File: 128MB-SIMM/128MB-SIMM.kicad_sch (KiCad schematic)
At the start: 6 parts

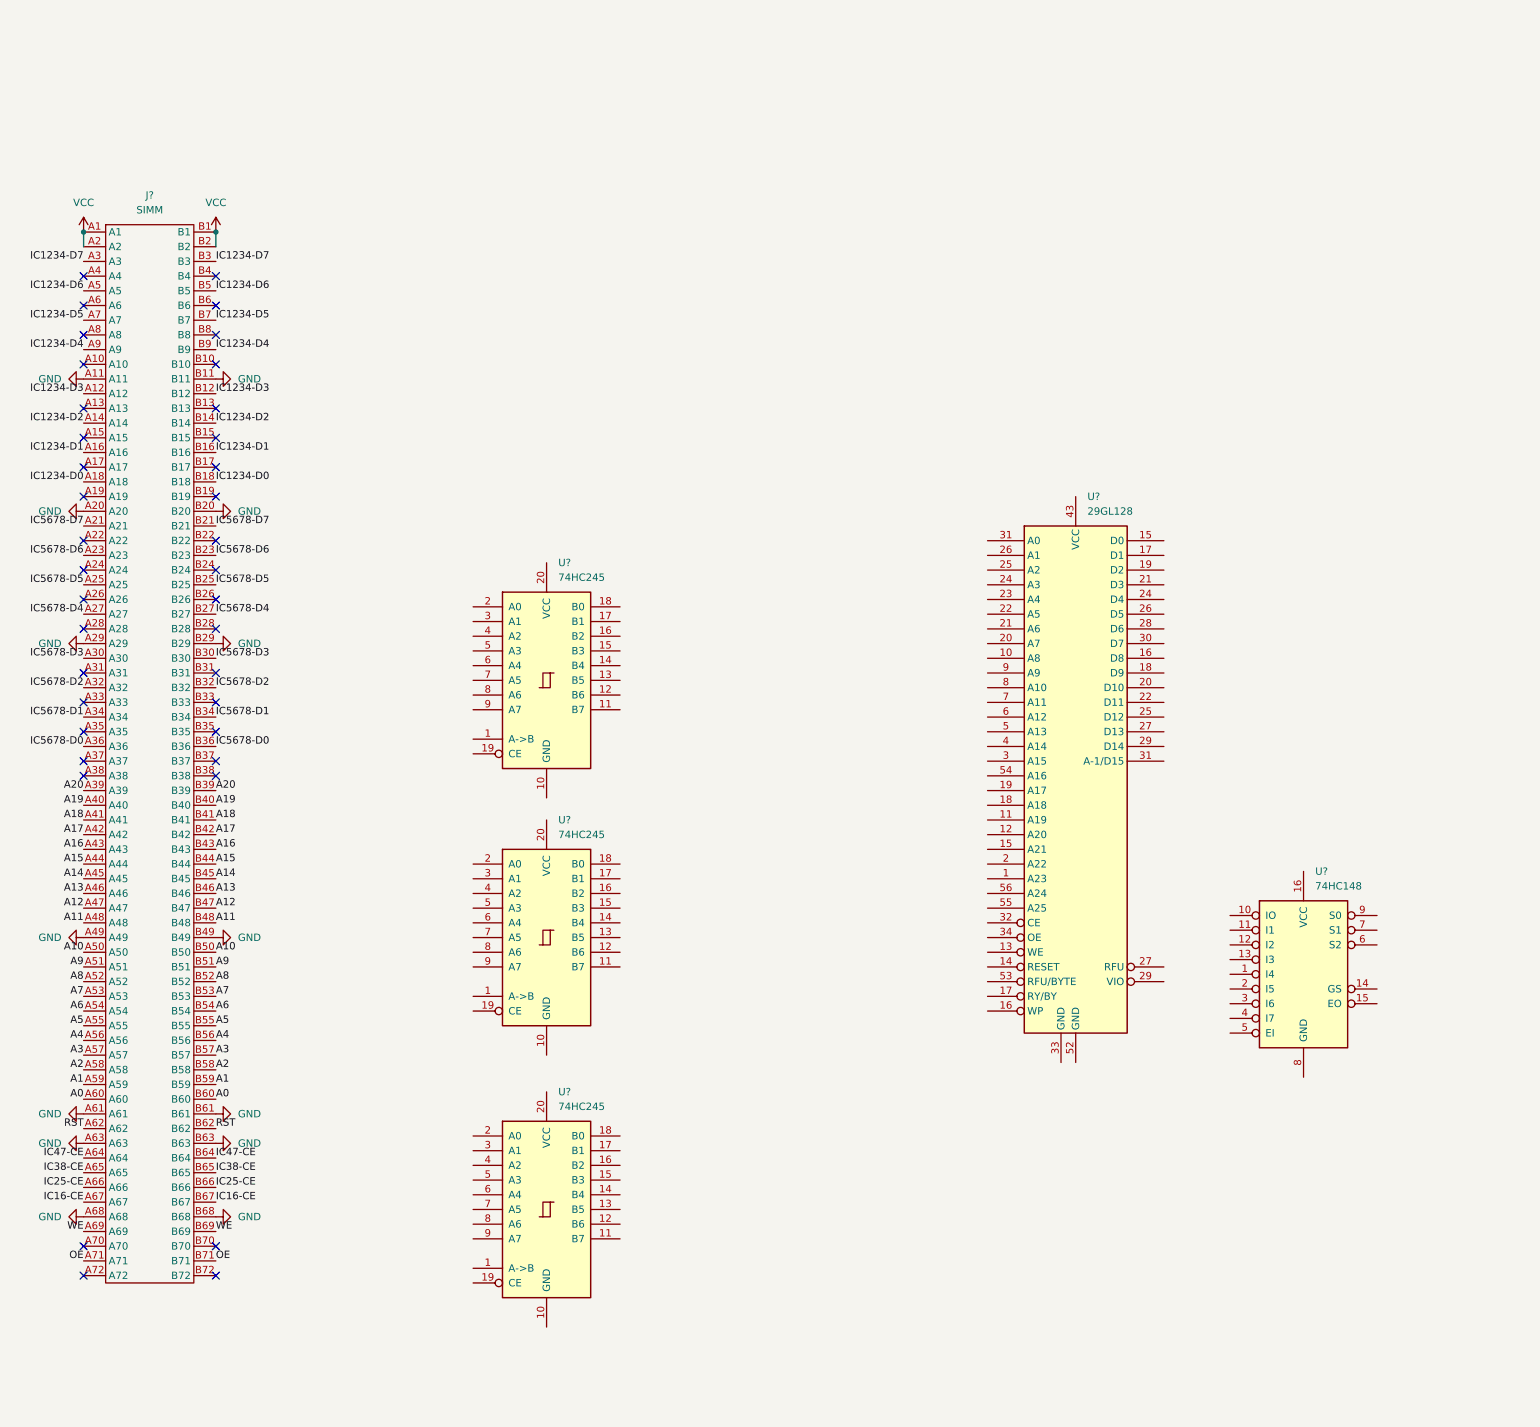
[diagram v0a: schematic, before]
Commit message: Updated 128 SIMM for release
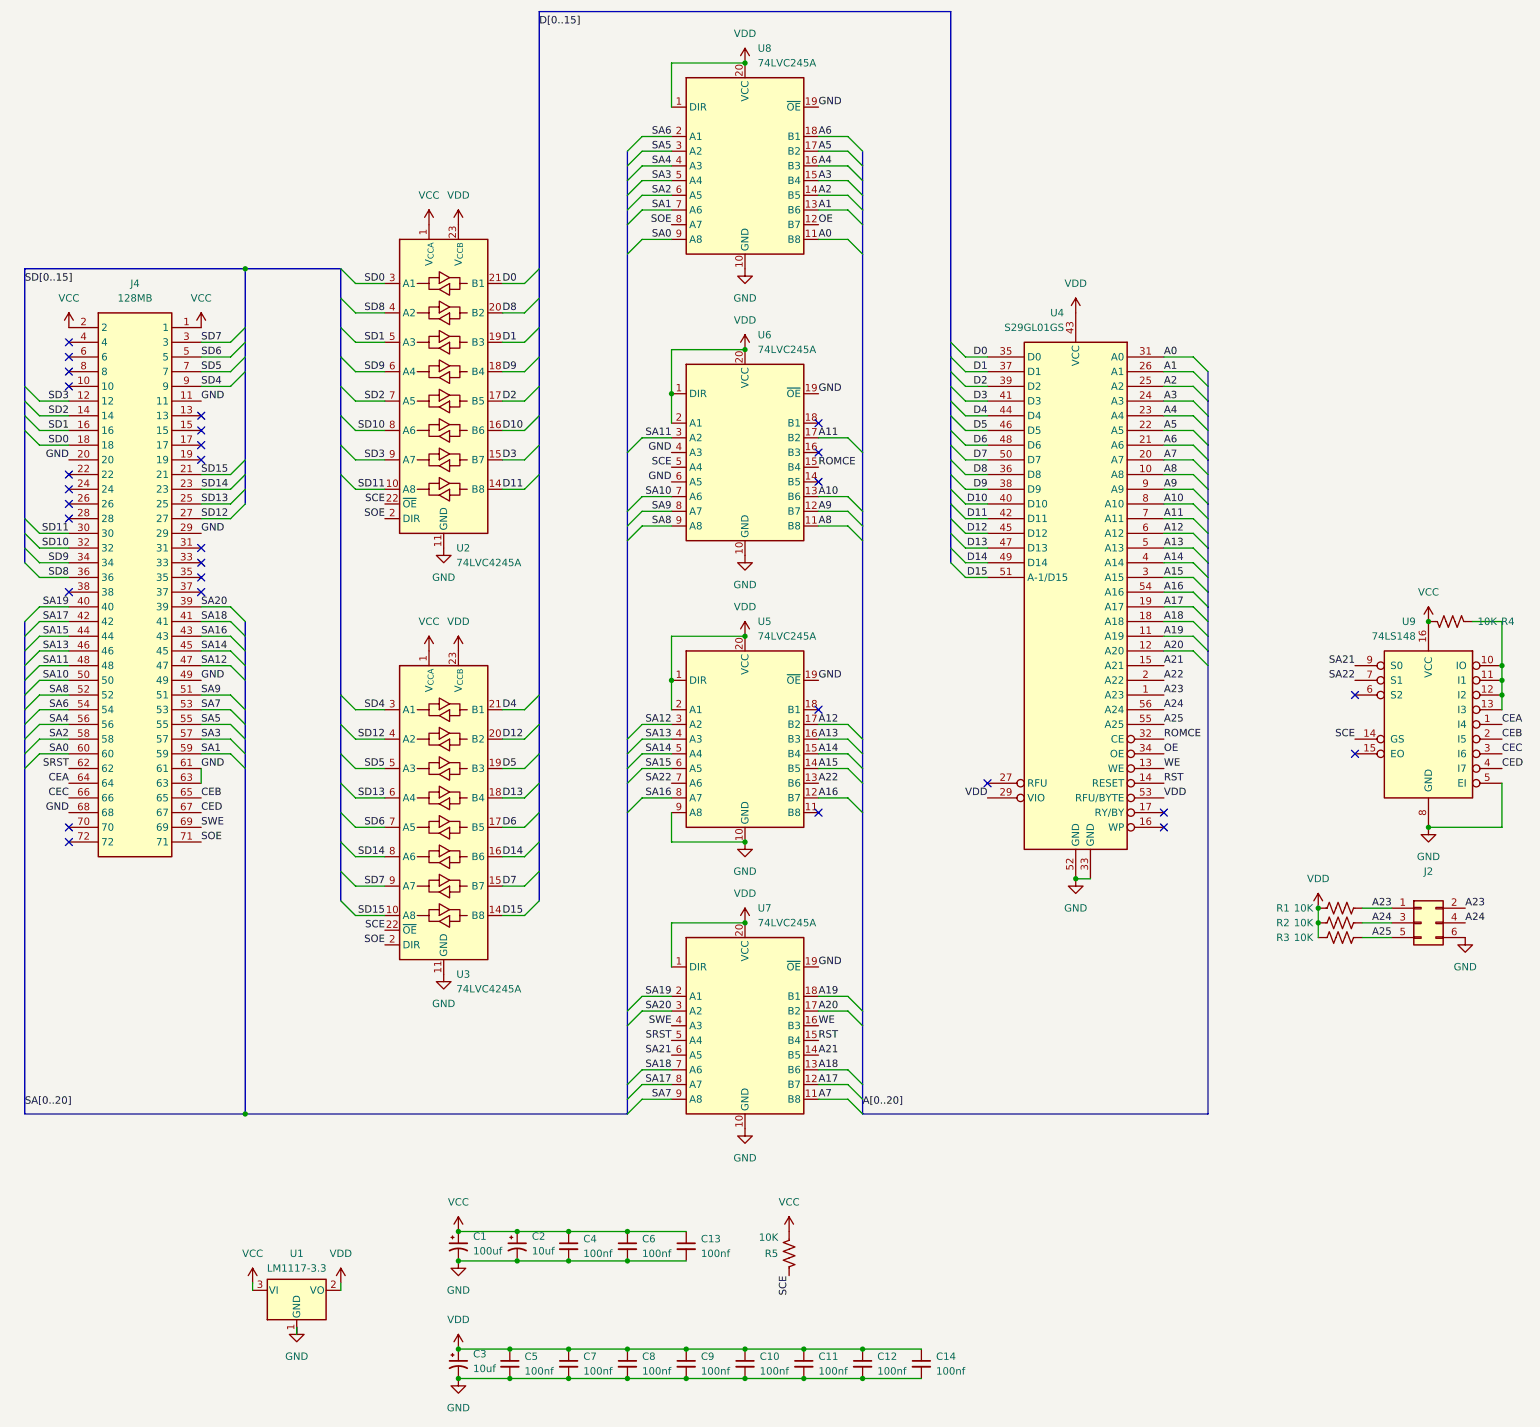
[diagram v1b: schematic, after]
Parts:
- removed J?: SIMM, symbol CPS3:SIMM
- added C1: 100uf, Capacitor_Tantalum_SMD:CP_EIA-3528-12_Kemet-T, symbol Device:C_Polarized_Small_US
- added C10, C11, C12, C13, C14, C4, C5, C6, C7, C8, C9: 100nf, Capacitor_SMD:C_0603_1608Metric, symbol Device:C_Small
- added C2, C3: 10uf, Capacitor_Tantalum_SMD:CP_EIA-3216-10_Kemet-I, symbol Device:C_Polarized_Small_US
- added J2: Conn_02x03_Odd_Even, Connector_PinSocket_1.27mm:PinSocket_2x03_P1.27mm_Horizontal, symbol Connector_Generic:Conn_02x03_Odd_Even
- added J4: 128MB, CPS3:SIMM_EDGE, symbol 5822030-3:5822030-3
- added R1, R2, R3, R4, R5: 10K, Resistor_SMD:R_0603_1608Metric, symbol Device:R_US
- added U1: LM1117-3.3, Package_TO_SOT_SMD:SOT-223-3_TabPin2, symbol Regulator_Linear:AMS1117-3.3
- added U2, U3: 74LVC4245A, Package_SO:TSSOP-24_4.4x7.8mm_P0.65mm, symbol Logic_LevelTranslator:SN74LVC8T245
- added U8: 74LVC245A, Package_SO:TSSOP-20_4.4x6.5mm_P0.65mm, symbol Logic_LevelTranslator:SN74LVC245APW
- U4: renamed from U?; value 29GL128 -> S29GL01GS; LCSC (none) -> C2064354
- U5, U6, U7: renamed from U?; value 74HC245 -> 74LVC245A; footprint (none) -> Package_SO:TSSOP-20_4.4x6.5mm_P0.65mm; symbol 74xx:74HC245 -> Logic_LevelTranslator:SN74LVC245APW; LCSC (none) -> C7848
- U9: renamed from U?; value 74HC148 -> 74LS148; footprint (none) -> Package_SO:SOIC-16_3.9x9.9mm_P1.27mm; symbol CPS3:74HC148 -> 74xx:74LS148; LCSC (none) -> C2674594
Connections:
- net A0: now also U4.31 (A0), U8.11 (B8)
- net A1: now also U4.26 (A1), U8.13 (B6)
- net A10: now also U4.8 (A10), U6.13 (B6)
- net A11: now also U4.7 (A11), U6.17 (B2)
- net A12: now also U4.6 (A12), U5.17 (B2)
- net A13: now also U4.5 (A13), U5.16 (B3)
- net A14: now also U4.4 (A14), U5.15 (B4)
- net A15: now also U4.3 (A15), U5.14 (B5)
- net A16: now also U4.54 (A16), U5.12 (B7)
- net A17: now also U4.19 (A17), U7.12 (B7)
- net A18: now also U4.18 (A18), U7.13 (B6)
- net A19: now also U4.11 (A19), U7.18 (B1)
- net A2: now also U4.25 (A2), U8.14 (B5)
- net A20: now also U4.12 (A20), U7.17 (B2)
- net A3: now also U4.24 (A3), U8.15 (B4)
- net A4: now also U4.23 (A4), U8.16 (B3)
- net A5: now also U4.22 (A5), U8.17 (B2)
- net A6: now also U4.21 (A6), U8.18 (B1)
- net A7: now also U4.20 (A7), U7.11 (B8)
- net A8: now also U4.10 (A8), U6.11 (B8)
- net A9: now also U4.9 (A9), U6.12 (B7)
- net GND: now also U4.33 (GND), U4.52 (GND), U5.10 (GND), U5.19 (~{OE}), U5.9 (A8), U6.10 (GND), U6.19 (~{OE}), U6.4 (A3), U6.6 (A5), U7.10 (GND), U7.19 (~{OE}), U9.5 (EI), U9.8 (GND), C1.2, C10.2, C11.2, C12.2, C13.2, C14.2, C2.2, C3.2, C4.2, C5.2, C6.2, C7.2, C8.2, C9.2, J2.6 (Pin_6), J4.11, J4.20, J4.29, J4.49, J4.61, J4.63, J4.68, U1.1 (GND), U2.11 (GND), U2.12 (GND), U2.13 (GND), U3.11 (GND), U3.12 (GND), U3.13 (GND), U8.10 (GND), U8.19 (~{OE})
- net OE: now also U4.34 (OE), U8.12 (B7)
- net RST: now also U4.14 (RESET), U7.15 (B4)
- net VCC: now also U9.16 (VCC), C1.1, C13.1, C2.1, C4.1, C6.1, J4.1, J4.2, R4.2, R5.2, U1.3 (VI), U2.1 (V_{CCA}), U3.1 (V_{CCA})
- net WE: now also U4.13 (WE), U7.16 (B3)
- net VDD: now reaches U5.1 (DIR)
- net VDD: now also U4.29 (VIO), U4.43 (VCC), U4.53 (RFU/BYTE), U5.2 (A1), U5.20 (VCC), U6.1 (DIR), U6.2 (A1), U6.20 (VCC), U7.1 (DIR), U7.20 (VCC), C10.1, C11.1, C12.1, C14.1, C3.1, C5.1, C7.1, C8.1, C9.1, R1.1, R2.1, R3.1, U1.2 (VO), U2.23 (V_{CCB}), U2.24 (V_{CCB}), U3.23 (V_{CCB}), U3.24 (V_{CCB}), U8.1 (DIR), U8.20 (VCC)
- net A22: now reaches U5.13 (B6)
- net A22: now also U4.2 (A22)
- net SA12: now reaches U5.3 (A2)
- net SA12: now also J4.47
- net SA13: now reaches U5.4 (A3)
- net SA13: now also J4.46
- net SA14: now reaches U5.5 (A4)
- net SA14: now also J4.45
- net SA15: now reaches U5.6 (A5)
- net SA15: now also J4.44
- net SA22: now reaches U5.7 (A6)
- net SA22: now also U9.7 (S1)
- net SA16: now reaches U5.8 (A7)
- net SA16: now also J4.43
- net A23: now reaches U4.1 (A23)
- net A23: now also J2.1 (Pin_1), J2.2 (Pin_2), R1.2
- net A21: now reaches U4.15 (A21)
- net A21: now also U7.14 (B5)
- net ROMCE: now reaches U4.32 (CE)
- net ROMCE: now also U6.15 (B4)
- net A25: now reaches U4.55 (A25)
- net A25: now also J2.5 (Pin_5), R3.2
- net A24: now reaches U4.56 (A24)
- net A24: now also J2.3 (Pin_3), J2.4 (Pin_4), R2.2
- net SA11: now reaches U6.3 (A2)
- net SA11: now also J4.48
- net SCE: now reaches U6.5 (A4)
- net SCE: now also U9.14 (GS), R5.1, U2.22 (~{OE}), U3.22 (~{OE})
- net SA10: now reaches U6.7 (A6)
- net SA10: now also J4.50
- net SA9: now reaches U6.8 (A7)
- net SA9: now also J4.51
- net SA8: now reaches U6.9 (A8)
- net SA8: now also J4.52
- net SA19: now reaches U7.2 (A1)
- net SA19: now also J4.40
- net SA20: now reaches U7.3 (A2)
- net SA20: now also J4.39
- net SWE: now reaches U7.4 (A3)
- net SWE: now also J4.69
- net SRST: now reaches U7.5 (A4)
- net SRST: now also J4.62
- net SA21: now reaches U7.6 (A5)
- net SA21: now also U9.9 (S0)
- net SA18: now reaches U7.7 (A6)
- net SA18: now also J4.41
- net SA17: now reaches U7.8 (A7)
- net SA17: now also J4.42
- net SA7: now reaches U7.9 (A8)
- net SA7: now also J4.53
- net CEA: now reaches U9.1 (I4)
- net CEA: now also J4.64
- net at U9.10 (IO): now also U9.11 (I1), U9.12 (I2), U9.13 (I3), R4.1
- net CEB: now reaches U9.2 (I5)
- net CEB: now also J4.65
- net CEC: now reaches U9.3 (I6)
- net CEC: now also J4.66
- net CED: now reaches U9.4 (I7)
- net CED: now also J4.67
- new net D0: U2.21 (B1), U4.35 (D0)
- new net D1: U2.19 (B3), U4.37 (D1)
- new net D10: U2.16 (B6), U4.40 (D10)
- new net D11: U2.14 (B8), U4.42 (D11)
- new net D12: U3.20 (B2), U4.45 (D12)
- new net D13: U3.18 (B4), U4.47 (D13)
- new net D14: U3.16 (B6), U4.49 (D14)
- new net D15: U3.14 (B8), U4.51 (A-1/D15)
- new net D2: U2.17 (B5), U4.39 (D2)
- new net D3: U2.15 (B7), U4.41 (D3)
- new net D4: U3.21 (B1), U4.44 (D4)
- new net D5: U3.19 (B3), U4.46 (D5)
- new net D6: U3.17 (B5), U4.48 (D6)
- new net D7: U3.15 (B7), U4.50 (D7)
- new net D8: U2.20 (B2), U4.36 (D8)
- new net D9: U2.18 (B4), U4.38 (D9)
- new net SA0: J4.60, U8.9 (A8)
- new net SA1: J4.59, U8.7 (A6)
- new net SA2: J4.58, U8.6 (A5)
- new net SA3: J4.57, U8.5 (A4)
- new net SA4: J4.56, U8.4 (A3)
- new net SA5: J4.55, U8.3 (A2)
- new net SA6: J4.54, U8.2 (A1)
- new net SD0: J4.18, U2.3 (A1)
- new net SD1: J4.16, U2.5 (A3)
- new net SD10: J4.32, U2.8 (A6)
- new net SD11: J4.30, U2.10 (A8)
- new net SD12: J4.27, U3.4 (A2)
- new net SD13: J4.25, U3.6 (A4)
- new net SD14: J4.23, U3.8 (A6)
- new net SD15: J4.21, U3.10 (A8)
- new net SD2: J4.14, U2.7 (A5)
- new net SD3: J4.12, U2.9 (A7)
- new net SD4: J4.9, U3.3 (A1)
- new net SD5: J4.7, U3.5 (A3)
- new net SD6: J4.5, U3.7 (A5)
- new net SD7: J4.3, U3.9 (A7)
- new net SD8: J4.36, U2.4 (A2)
- new net SD9: J4.34, U2.6 (A4)
- new net SOE: J4.71, U2.2 (DIR), U3.2 (DIR), U8.8 (A7)
- no-connect marks 38 -> 29
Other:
- moved on the sheet: U4, U9
